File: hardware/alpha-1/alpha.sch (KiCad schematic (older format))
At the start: 82 parts, among them J1 POWER, J2 SERIAL, P1 SWITCH_1, P2 SWITCH_2, P3 SWITCH_3, P4 SWITCH_4, P5 SWITCH_5, P6 SWITCH_6, P7 INPUTS, P8 RASPBERRY_PI, P9 12V, Q1 DMN2041L-7, Q2 DMN2041L-7, Q3 DMN2041L-7, Q4 DMN2041L-7, Q5 DMN2041L-7, Q6 DMN2041L-7, U1 TPS54202, U2 TMP102

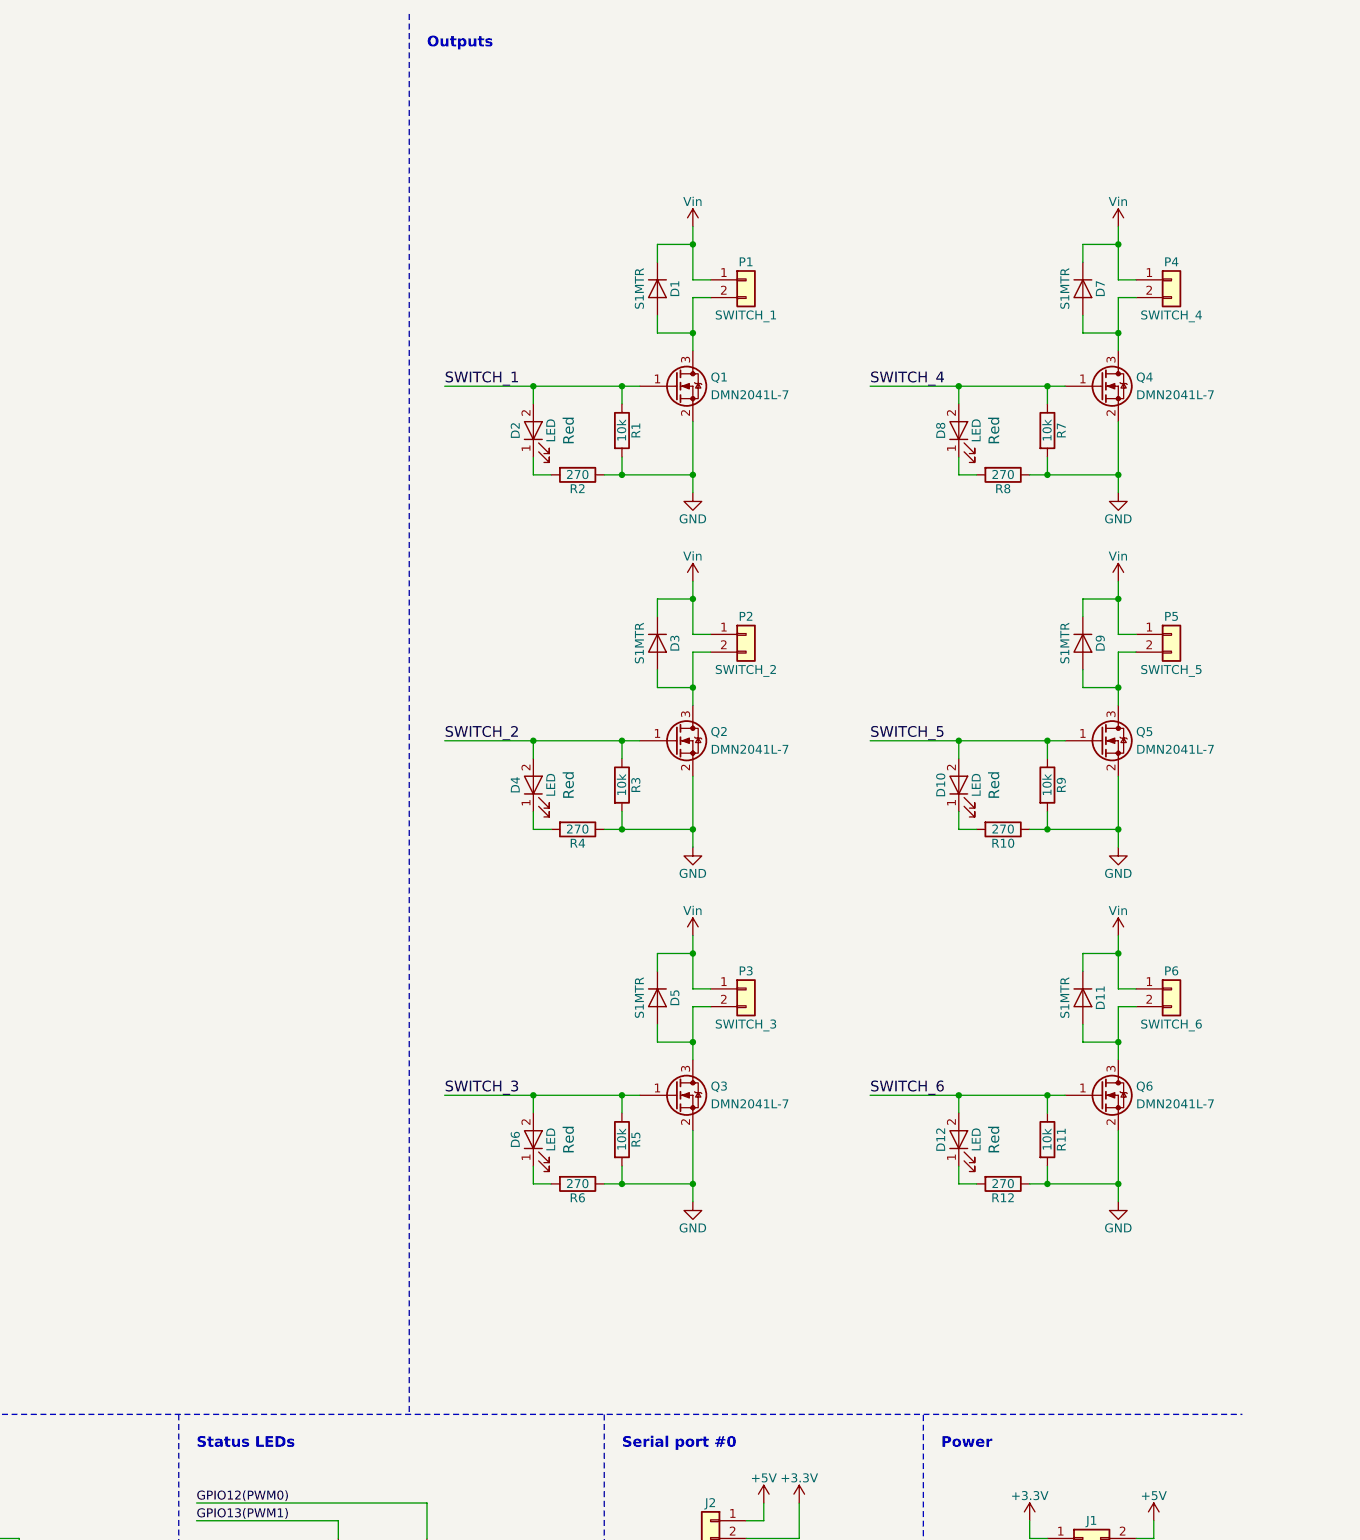
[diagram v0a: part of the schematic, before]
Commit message: o Changing connectors from Phoenix PTSM to Harting har-flexicon. o Combing all outputs into a single output terminal to save some space. Will make up for it with slik print.
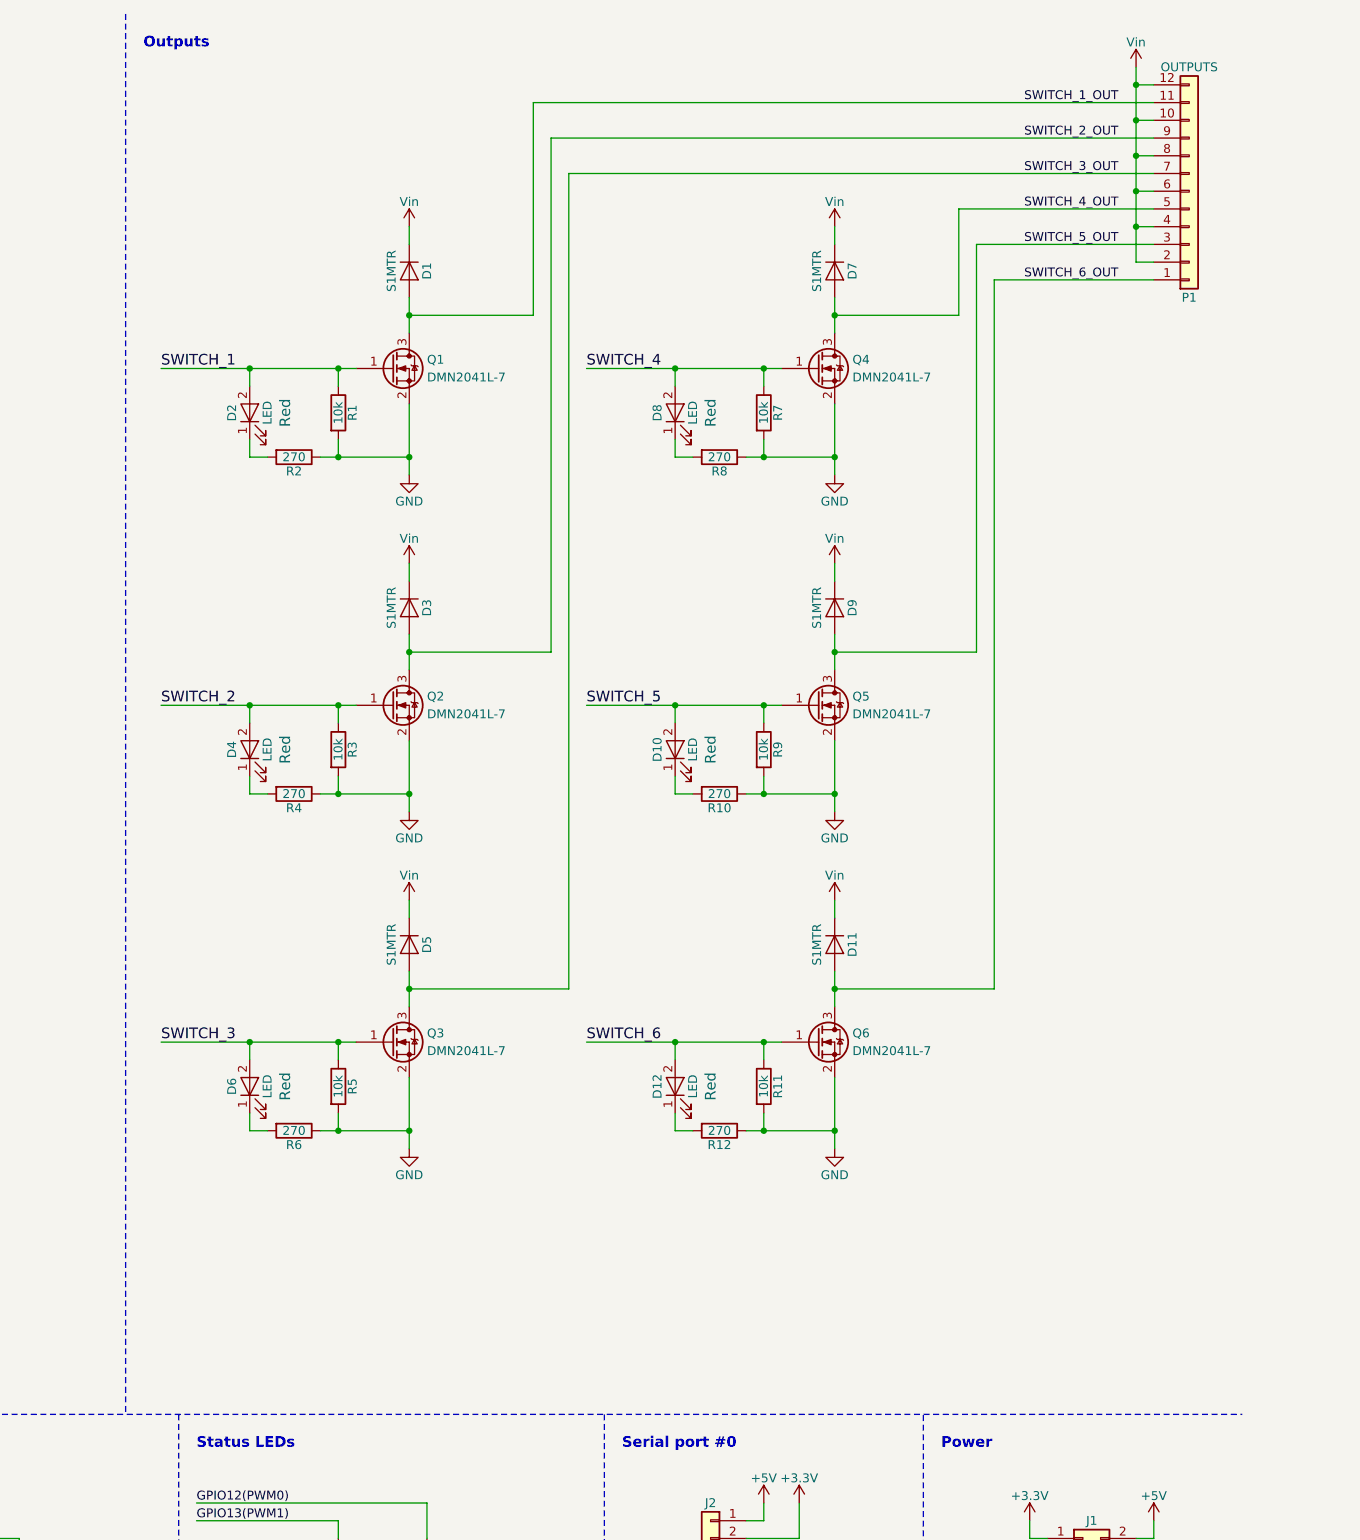
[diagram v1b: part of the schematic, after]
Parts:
- removed P1: SWITCH_1, Bitraf:PhoenixContact_PTSM_0,5_2-2,5-H_SMD, symbol Conn_01x02
- removed P2: SWITCH_2, Bitraf:PhoenixContact_PTSM_0,5_2-2,5-H_SMD, symbol Conn_01x02
- removed P3: SWITCH_3, Bitraf:PhoenixContact_PTSM_0,5_2-2,5-H_SMD, symbol Conn_01x02
- removed P4: SWITCH_4, Bitraf:PhoenixContact_PTSM_0,5_2-2,5-H_SMD, symbol Conn_01x02
- removed P5: SWITCH_5, Bitraf:PhoenixContact_PTSM_0,5_2-2,5-H_SMD, symbol Conn_01x02
- removed P6: SWITCH_6, Bitraf:PhoenixContact_PTSM_0,5_2-2,5-H_SMD, symbol Conn_01x02
- added P1: OUTPUTS, Bitraf:har-flexicon_2,54_TSPH-12_T56_BK, symbol Conn_01x12
- P7: footprint Bitraf:PhoenixContact_PTSM_0,5_8-2,5-H_SMD -> Bitraf:har-flexicon_2,54_TSPH-08_T56_BK; mpn 1771088 -> (none)
- P9: footprint Bitraf:PhoenixContact_PTSM_0,5_2-2,5-H_SMD -> Bitraf:har-flexicon_2,54_TSPH-02_T56_BK; mpn 1702473 -> (none)
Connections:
- net Vin: now also P1.10 (Pin_10), P1.12 (Pin_12), P1.2 (Pin_2), P1.4 (Pin_4), P1.6 (Pin_6), P1.8 (Pin_8)
- net SWITCH_2_OUT: now reaches D3.2 (A), Q2.3 (D)
- net SWITCH_2_OUT: now also P1.9 (Pin_9)
- net SWITCH_1_OUT: now reaches D1.2 (A), Q1.3 (D)
- net SWITCH_1_OUT: now also P1.11 (Pin_11)
- net SWITCH_3_OUT: now reaches D5.2 (A), Q3.3 (D)
- net SWITCH_3_OUT: now also P1.7 (Pin_7)
- net SWITCH_4_OUT: now reaches D7.2 (A), Q4.3 (D)
- net SWITCH_4_OUT: now also P1.5 (Pin_5)
- net SWITCH_5_OUT: now reaches D9.2 (A), Q5.3 (D)
- net SWITCH_5_OUT: now also P1.3 (Pin_3)
- net SWITCH_6_OUT: now reaches D11.2 (A), Q6.3 (D)
- net SWITCH_6_OUT: now also P1.1 (Pin_1)
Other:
- moved on the sheet: D1, D10, D11, D12, D2, D3, D4, D5, D6, D7, D8, D9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

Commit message: o Routing most of the board.
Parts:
- removed P8: RASPBERRY_PI, symbol Conn_02x20_Odd_Even
- added U3: RASPBERRY_PI, Socket_Strips:Socket_Strip_Straight_2x20_Pitch2.54mm, symbol RASPBERRY_PI
- C1, C3, C5, C6: footprint Capacitors_SMD:C_0805 -> IPC7351-Nominal:CAPC2012X70
- C4: footprint Capacitors_SMD:C_0805 -> IPC7351-Nominal:CAPC1005X55; mpn 08051A750JAT2A -> GRM1555C1H750JA01D
- D21: value LED -> POWER
- D22: value LED -> STATUS_1
- D23: value LED -> STATUS_2
- R21: footprint Resistors_SMD:R_0805 -> IPC7351-Nominal:RESC1005X38; mpn RC0805FR-07100KL -> RC0402FR-07100KL
- R22: footprint Resistors_SMD:R_0805 -> IPC7351-Nominal:RESC1005X38; mpn RC0805FR-0713K3L -> RC0402FR-0713K3L
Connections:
- net +12V is gone; now on net Vin: C2.1, C3.1, P9.1 (Pin_1), U1.3 (Vin)
- net +3V3: now also U3.1 (3.3V), U3.17 (3.3V)
- net +5V: now also U3.2 (5V), U3.4 (5V)
- net GND: now also U3.14 (GND), U3.20 (GND), U3.25 (GND), U3.30 (GND), U3.34 (GND), U3.39 (GND), U3.6 (GND), U3.9 (GND)
- net INPUT_1: now also U3.22 (GPIO25/GEN6)
- net INPUT_2: now also U3.19 (GPIO10/SPI0_MOSI)
- net INPUT_3: now also U3.18 (GPIO24/GEN5)
- net INPUT_4: now also U3.15 (GPIO22/GEN3)
- net INPUT_5: now also U3.16 (GPIO23/GEN4)
- net INPUT_6: now also U3.13 (GPIO27/GEN2)
- net INPUT_7: now also U3.12 (GPIO18/GEN1/PWM0)
- net INPUT_8: now also U3.11 (GPIO17/GEN0)
- net SWITCH_1: now also U3.31 (GPIO6)
- net SWITCH_2: now also U3.35 (GPIO19/SPI1_MISO)
- net SWITCH_3: now also U3.36 (GPIO16)
- net SWITCH_4: now also U3.37 (GPIO26)
- net SWITCH_5: now also U3.38 (GPIO20/SPI1_MOSI)
- net SWITCH_6: now also U3.40 (GPIO21/SPI1_SCK)
- net SW: now reaches C1.2, L1.2, U1.2 (SW)
- net FB: now reaches C4.2, R21.2, R22.1, U1.4 (FB)
- net BOOT: now reaches C1.1, U1.6 (BOOT)
- net GPIO12(PWM0) renamed STATUS_LED_1
- net STATUS_LED_1: now also U3.32 (GPIO12/PWM0)
- net GPIO13(PWM1) renamed STATUS_LED_2
- net STATUS_LED_2: now also U3.33 (GPIO13/PWM1)
- net GPIO14(TXD0) renamed SERIAL_TX
- net SERIAL_TX: now also U3.8 (GPIO14/TXD0)
- net GPIO15(RXD0) renamed SERIAL_RX
- net SERIAL_RX: now also U3.10 (GPIO15/RXD0)
- net GPIO16 renamed TMP102_PWR
- net TMP102_PWR: now also U3.7 (GPIO4/GCLK)
- net GPIO2(SDA1) renamed TMP102_SDA
- net TMP102_SDA: now also U3.3 (GPIO2/SDA1)
- net GPIO3(SCL1) renamed TMP102_SCL
- net TMP102_SCL: now also U3.5 (GPIO3/SCL1)
- no-connect marks 3 -> 4
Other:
- moved on the sheet: D11, D12, D3, D4, D5, D6, D7, D8, P1, P9, Q2, Q3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

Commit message: o Routing complete. o Adding some print. o Milling out area around TMP102.
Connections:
- net ~TMP102_ALERT: now reaches R26.2, U2.3 (ALERT)
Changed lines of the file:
@@
 	8600 9700 9800 9700
 Wire Wire Line
-	8600 9900 9100 9900
+	8600 9900 9800 9900
 Wire Wire Line
 	8700 9500 8700 9700
@@
 Text Label 3900 9900 0    60   ~ 0
 FB
+Text Label 9800 9900 2    60   ~ 0
+~TMP102_ALERT
+Connection ~ 9100 9900
 $EndSCHEMATC

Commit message: o Fixing the rest of the missing components. o Ready for production.
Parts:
- D1, D11, D3, D5, D7, D9: digikey 1655-1506-2-ND -> 1655-1506-1-ND
- J1, J2, MK1, MK2, MK3, MK4, TP1: assembly (none) -> footprint only
- P1: mpn (none) -> 14011213102000
- P2: renamed from P7; mpn (none) -> 14010813102000
- P3: renamed from U3; mpn (none) -> PPTC202LFBN-RC
- P4: renamed from P9; mpn (none) -> 14010213102000
- R1, R11, R13, R14, R15, R16, R17, R18, R19, R20, R24, R25, R26, R3, R5, R7, R9: mpn (none) -> RMCF0402FT10K0
- R10, R12, R2, R4, R6, R8: mpn (none) -> RC1005F271CS
- R23, R27, R28: mpn (none) -> RC1005F561CS
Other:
- note removed: "TODO: extension header hvis lett\n"

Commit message: hardware: Add reverse polarity protection and fix output silkscreen
Using a SOD-123 (MINISMA) diode like
https://www.digikey.no/product-detail/en/comchip-technology/CDBM140-G/641-1325-1-ND/1979690

Note: Using Kicad5, might not be compatible with KiCad4 anymore
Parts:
- added D24: CDBM140-G, Diodes_SMD:D_SOD-123, symbol device:D_Schottky
- C1, C2, C3, C4, C5, C6: symbol C -> device:C
- D1, D11, D3, D5, D7, D9: symbol D -> device:D
- D10, D12, D2, D21, D22, D23, D4, D6, D8: symbol LED -> device:LED
- D13, D14, D15, D16, D17, D18, D19, D20: symbol D_Zener -> device:D_Zener
- J1: symbol Conn_02x02_Odd_Even -> conn:Conn_02x02_Odd_Even
- J2: symbol Conn_01x05 -> conn:Conn_01x05
- L1: symbol L_Core_Ferrite -> device:L_Core_Ferrite
- MK1, MK2, MK3, MK4: symbol Mounting_Hole -> mechanical:Mounting_Hole
- P1: symbol Conn_01x12 -> conn:Conn_01x12
- P2: symbol Conn_01x08 -> conn:Conn_01x08
- P3: symbol RASPBERRY_PI -> alpha-misc:RASPBERRY_PI
- P4: symbol Conn_01x02 -> conn:Conn_01x02
- Q1, Q2, Q3, Q4, Q5, Q6: symbol Q_NMOS_GSD -> device:Q_NMOS_GSD
- R1, R10, R11, R12, R13, R14, R15, R16, R17, R18, R19, R2, R20, R21, R22, R23, R24, R25, R26, R27, R28, R3, R4, R5, R6, R7, R8, R9: symbol R -> device:R
- TP1: symbol TEST_1P -> conn:TEST_1P
- U1: symbol TPS54202 -> tps54202:TPS54202
- U2: symbol TMP102 -> tmp102:TMP102
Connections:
- wire segments 248 -> 323
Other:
- moved on the sheet: P4
